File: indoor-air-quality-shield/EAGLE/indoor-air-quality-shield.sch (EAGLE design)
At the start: 42 parts, among them IC1 LM358D, IC2 LM358D, Q1 MMBT2222A, Q2 MMBT2222A, Q3 MMBT2222A

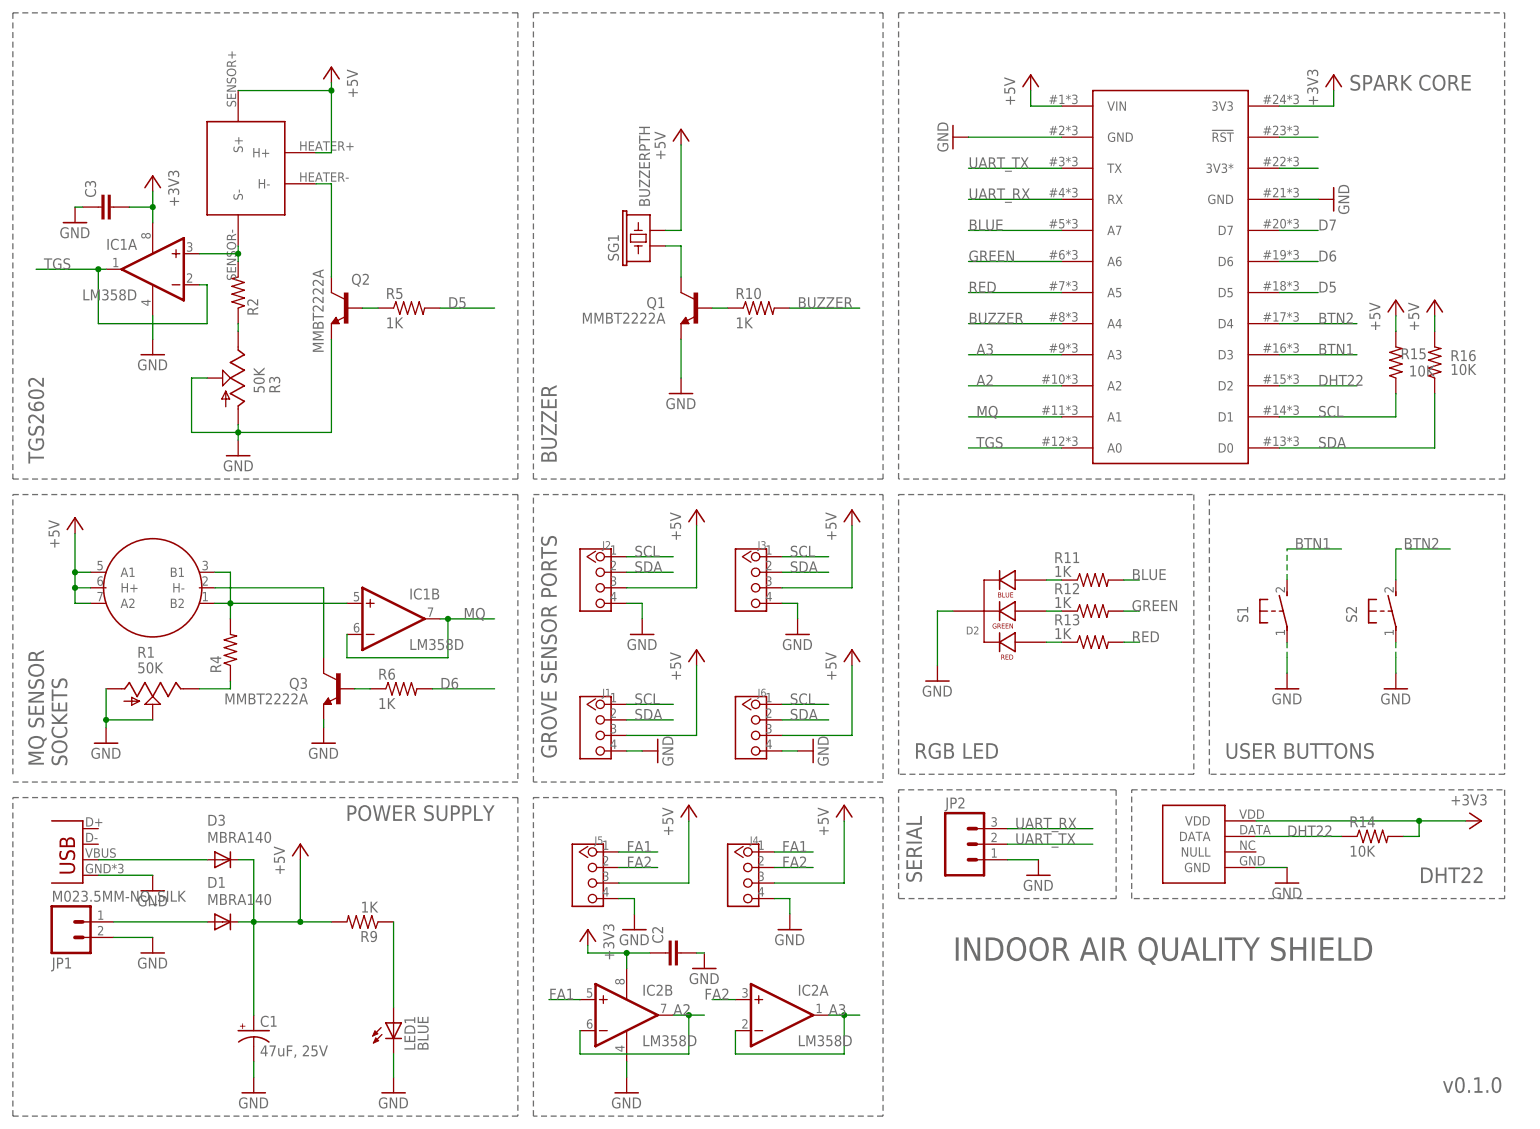
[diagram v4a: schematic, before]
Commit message: added bypass caps and labeled connectors
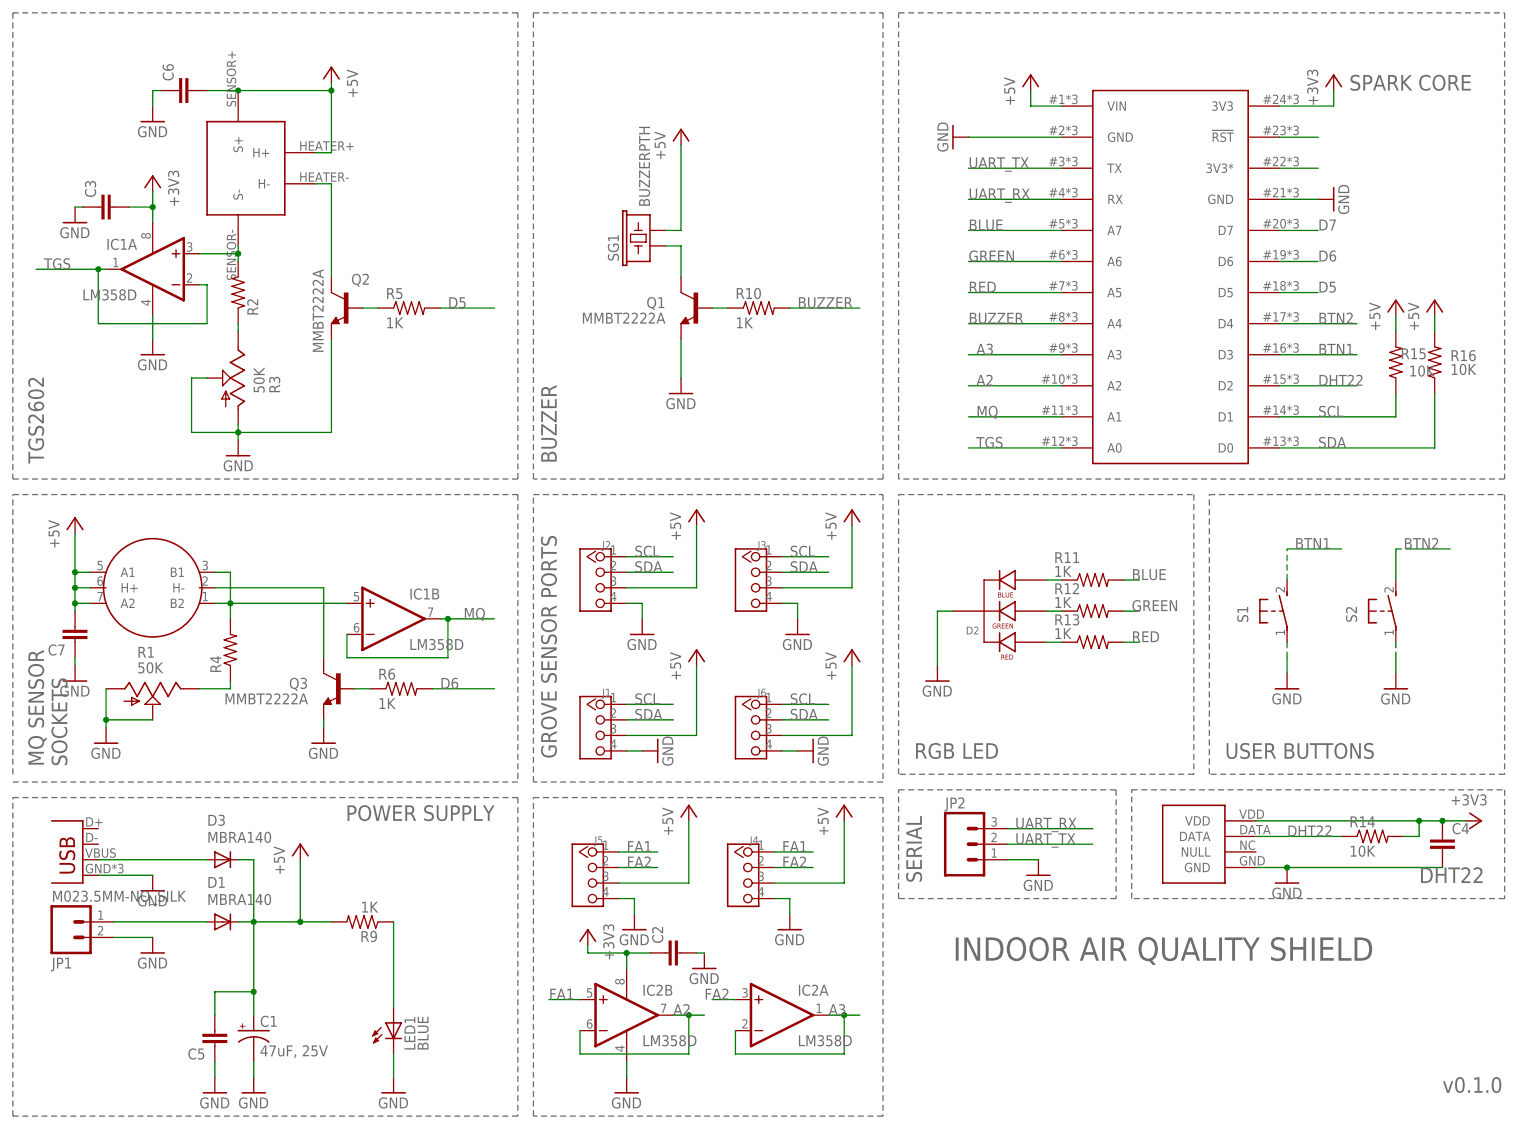
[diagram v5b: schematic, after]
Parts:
- added C4, C5, C6, C7: (no value), rcl:C-EUC0603
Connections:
- net +3V3: now also C4.1
- net +5V: now also C5.2, C6.2, C7.2
- net GND: now also C4.2, C5.1, C6.1, C7.1
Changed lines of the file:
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@@
 <setting verticaltext="up"/>
 </settings>
-<grid distance="0.1" unitdist="inch" unit="inch" style="lines" multiple="1" display="no" altdistance="0.01" altunitdist="inch" altunit="inch"/>
+<grid distance="0.05" unitdist="inch" unit="inch" style="lines" multiple="1" display="yes" altdistance="0.01" altunitdist="inch" altunit="inch"/>
 <layers>
 <layer number="1" name="Top" color="4" fill="1" visible="no" active="no"/>
@@
 <part name="GND24" library="supply1" deviceset="GND" device=""/>
 <part name="GND25" library="supply1" deviceset="GND" device=""/>
+<part name="C4" library="rcl" deviceset="C-EU" device="C0603"/>
+<part name="C5" library="rcl" deviceset="C-EU" device="C0603"/>
+<part name="GND26" library="supply1" deviceset="GND" device=""/>
+<part name="C6" library="rcl" deviceset="C-EU" device="C0603"/>
+<part name="C7" library="rcl" deviceset="C-EU" device="C0603"/>
+<part name="GND27" library="supply1" deviceset="GND" device=""/>
+<part name="GND28" library="supply1" deviceset="GND" device=""/>
 </parts>
 <sheets>
@@
 <instance part="GND24" gate="1" x="12.7" y="148.59"/>
 <instance part="GND25" gate="1" x="115.57" y="26.67"/>
+<instance part="C4" gate="G$1" x="236.22" y="48.26"/>
+<instance part="C5" gate="G$1" x="35.56" y="13.97" rot="R180"/>
+<instance part="GND26" gate="1" x="35.56" y="6.35"/>
+<instance part="C6" gate="G$1" x="29.21" y="170.18" rot="R90"/>
+<instance part="C7" gate="G$1" x="12.7" y="80.01" rot="R180"/>
+<instance part="GND27" gate="1" x="25.4" y="165.1"/>
+<instance part="GND28" gate="1" x="12.7" y="73.66"/>
 </instances>
 <busses>
@@
 <pinref part="GND22" gate="1" pin="GND"/>
 <wire x1="205.74" y1="43.18" x2="210.82" y2="43.18" width="0.1524" layer="91"/>
+<pinref part="C4" gate="G$1" pin="2"/>
+<wire x1="210.82" y1="43.18" x2="236.22" y2="43.18" width="0.1524" layer="91"/>
+<junction x="210.82" y="43.18"/>
 </segment>
 <segment>
@@
 <pinref part="GND25" gate="1" pin="GND"/>
 <wire x1="115.57" y1="29.21" x2="114.3" y2="29.21" width="0.1524" layer="91"/>
+</segment>
+<segment>
+<pinref part="C5" gate="G$1" pin="1"/>
+<pinref part="GND26" gate="1" pin="GND"/>
+<wire x1="35.56" y1="8.89" x2="35.56" y2="11.43" width="0.1524" layer="91"/>
+</segment>
+<segment>
+<pinref part="GND27" gate="1" pin="GND"/>
+<pinref part="C6" gate="G$1" pin="1"/>
+<wire x1="25.4" y1="167.64" x2="25.4" y2="170.18" width="0.1524" layer="91"/>
+<wire x1="25.4" y1="170.18" x2="26.67" y2="170.18" width="0.1524" layer="91"/>
+</segment>
+<segment>
+<pinref part="C7" gate="G$1" pin="1"/>
+<pinref part="GND28" gate="1" pin="GND"/>
+<wire x1="12.7" y1="76.2" x2="12.7" y2="77.47" width="0.1524" layer="91"/>
 </segment>
 </net>
@@
 <wire x1="54.61" y1="171.45" x2="54.61" y2="170.18" width="0.1524" layer="91"/>
 <junction x="54.61" y="170.18"/>
+<pinref part="C6" gate="G$1" pin="2"/>
+<wire x1="34.29" y1="170.18" x2="39.37" y2="170.18" width="0.1524" layer="91"/>
+<junction x="39.37" y="170.18"/>
 </segment>
 <segment>
@@
 <wire x1="12.7" y1="97.79" x2="12.7" y2="91.44" width="0.1524" layer="91"/>
 <junction x="12.7" y="91.44"/>
+<pinref part="C7" gate="G$1" pin="2"/>
+<wire x1="12.7" y1="85.09" x2="12.7" y2="86.36" width="0.1524" layer="91"/>
+<junction x="12.7" y="86.36"/>
 </segment>
 <segment>
@@
 <wire x1="39.37" y1="34.29" x2="41.91" y2="34.29" width="0.1524" layer="91"/>
 <pinref part="C1" gate="G$1" pin="+"/>
-<wire x1="41.91" y1="19.05" x2="41.91" y2="34.29" width="0.1524" layer="91"/>
+<wire x1="41.91" y1="19.05" x2="41.91" y2="22.86" width="0.1524" layer="91"/>
 <junction x="41.91" y="34.29"/>
+<wire x1="41.91" y1="22.86" x2="41.91" y2="34.29" width="0.1524" layer="91"/>
 <wire x1="41.91" y1="34.29" x2="49.53" y2="34.29" width="0.1524" layer="91"/>
 <pinref part="D3" gate="G$1" pin="C"/>
 <wire x1="39.37" y1="44.45" x2="41.91" y2="44.45" width="0.1524" layer="91"/>
 <wire x1="41.91" y1="44.45" x2="41.91" y2="34.29" width="0.1524" layer="91"/>
+<pinref part="C5" gate="G$1" pin="2"/>
+<wire x1="35.56" y1="19.05" x2="35.56" y2="22.86" width="0.1524" layer="91"/>
+<wire x1="35.56" y1="22.86" x2="41.91" y2="22.86" width="0.1524" layer="91"/>
+<junction x="41.91" y="22.86"/>
 </segment>
 <segment>
@@
 <pinref part="+3V2" gate="G$1" pin="+3V3"/>
 <pinref part="R14" gate="G$1" pin="2"/>
-<wire x1="232.41" y1="50.8" x2="240.03" y2="50.8" width="0.1524" layer="91"/>
+<wire x1="232.41" y1="50.8" x2="236.22" y2="50.8" width="0.1524" layer="91"/>
+<wire x1="236.22" y1="50.8" x2="240.03" y2="50.8" width="0.1524" layer="91"/>
 <wire x1="229.87" y1="48.26" x2="232.41" y2="48.26" width="0.1524" layer="91"/>
 <wire x1="232.41" y1="48.26" x2="232.41" y2="50.8" width="0.1524" layer="91"/>
 <junction x="232.41" y="50.8"/>
-</segment>
-<segment>
+<pinref part="C4" gate="G$1" pin="1"/>
+<junction x="236.22" y="50.8"/>
+</segment>
+<segment>
